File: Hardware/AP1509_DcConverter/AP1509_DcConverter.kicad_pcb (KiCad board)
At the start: 4 copper layers, 34 x 34 mm, 17 parts, among them J2 01x02, J3 01x03, U1 AP1509

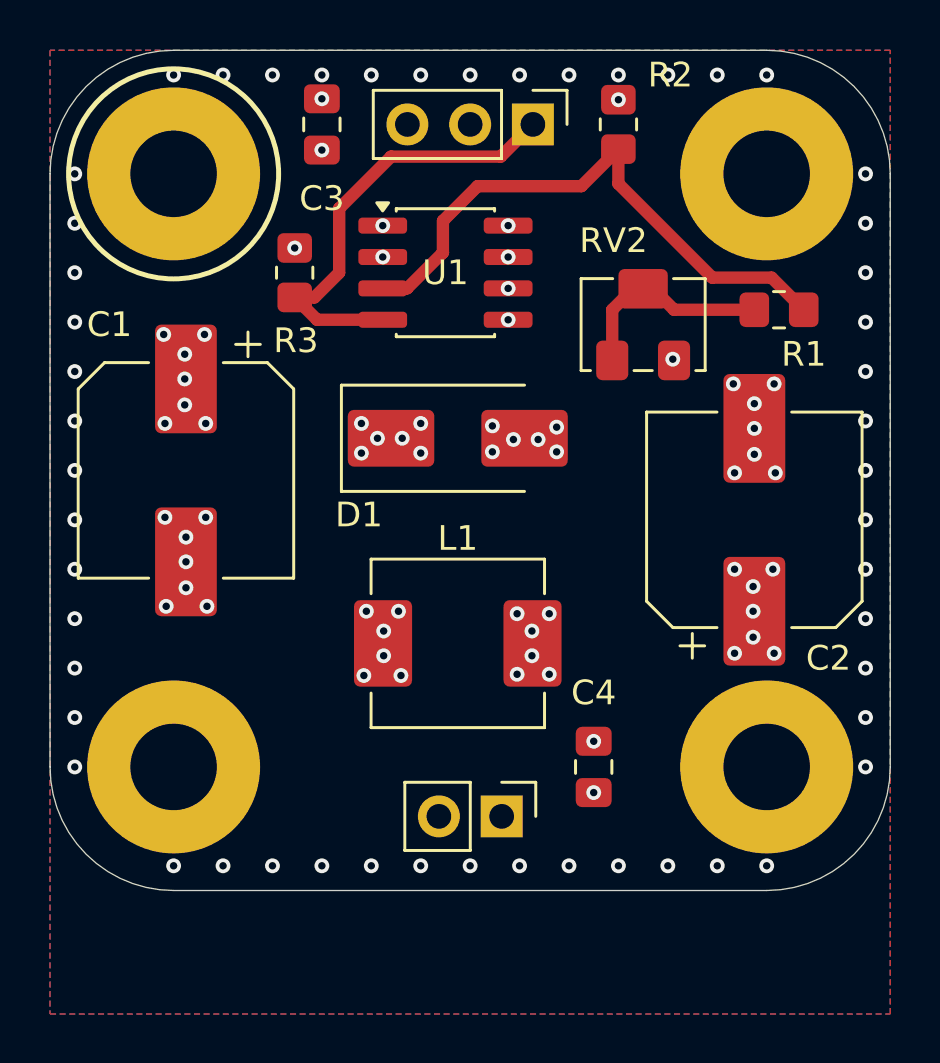
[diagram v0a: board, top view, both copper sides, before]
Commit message: Hardware updates. Add Lr04 lora module datasheets
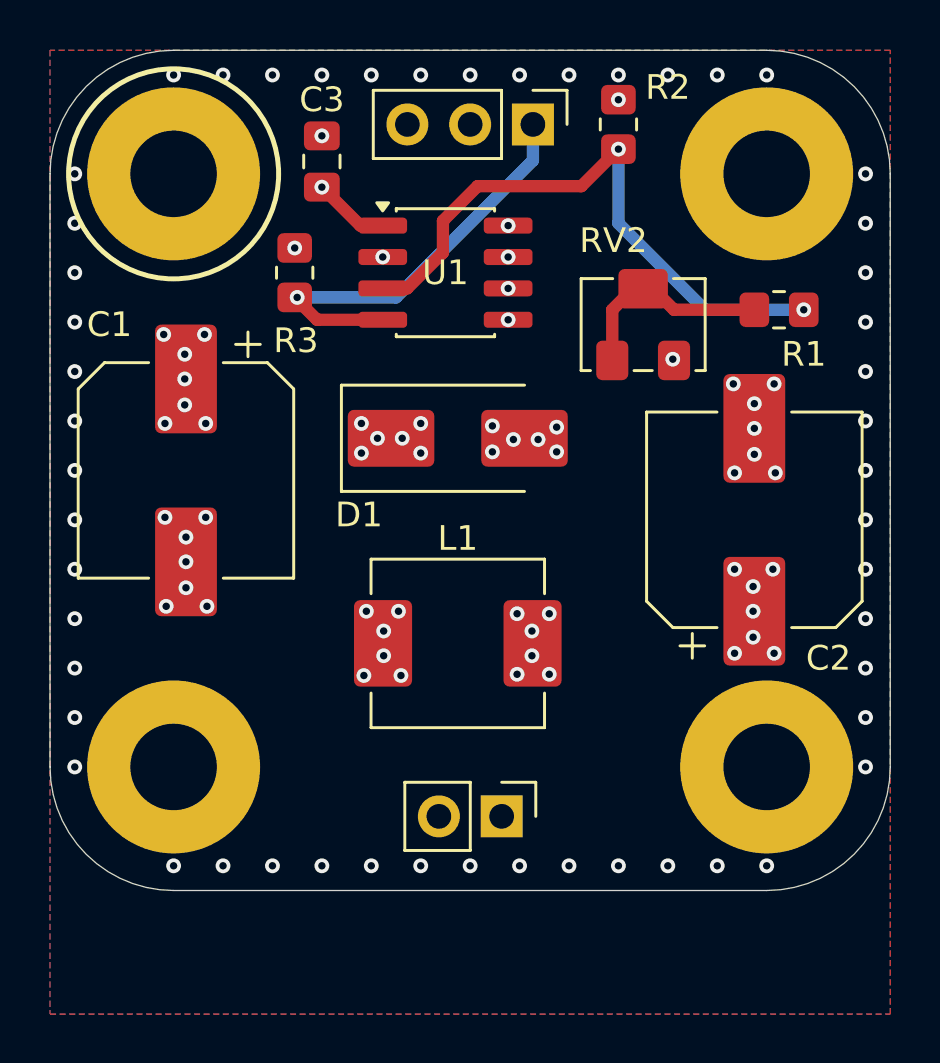
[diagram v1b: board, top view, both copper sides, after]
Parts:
- removed C4: 0.1uF, Capacitor_SMD:C_0805_2012Metric_Pad1.18x1.45mm_HandSolder
- moved C3 1.50 mm to (134.0, 63.5)
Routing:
- net Net-(J3-Pin_3): track 0.00 -> 3.11 mm, vias 9 -> 8
- net Net-(U1-FB): track 23.6 -> 24.6 mm, vias 0 -> 2
- net Net-(J3-Pin_1): track 18.0 -> 17.3 mm, vias 0 -> 1
- net Net-(J2-Pin_1): vias 15 -> 14
- net GND: vias 80 -> 79
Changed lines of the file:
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@@
 	(paper "A4")
 	(layers
-		(0 "F.Cu" signal "Traces")
+		(0 "F.Cu" signal "F.Signal-Ground")
 		(4 "In1.Cu" power "Ground")
 		(6 "In2.Cu" mixed "Power")
-		(2 "B.Cu" power "Ground2")
+		(2 "B.Cu" power "B.Signal-Ground")
 		(5 "F.SilkS" user "F.Silkscreen")
 		(7 "B.SilkS" user "B.Silkscreen")
@@
 				(type "Top Silk Screen")
 			)
-			(layer "F.Paste"
-				(type "Top Solder Paste")
-			)
 			(layer "F.Mask"
 				(type "Top Solder Mask")
@@
 				(thickness 0.01)
 			)
-			(layer "B.Paste"
-				(type "Bottom Solder Paste")
-			)
 			(layer "B.SilkS"
 				(type "Bottom Silk Screen")
@@
 	(footprint "Capacitor_SMD:C_0805_2012Metric_Pad1.18x1.45mm_HandSolder"
 		(layer "F.Cu")
-		(at 134 62 90)
+		(at 134 63.5 90)
 		(descr "Capacitor SMD 0805 (2012 Metric), square (rectangular) end terminal, IPC-7351 nominal with elongated pad for handsoldering. (Body size source: IPC-SM-782 page 76, https://www.pcb-3d.com/wordpress/wp-content/uploads/ipc-sm-782a_amendment_1_and_2.pdf, https://docs.google.com/spreadsheets/d/1BsfQQcO9C6DZCsRaXUlFlo91Tg2WpOkGARC1WS5S8t0/edit?usp=sharing), generated with kicad-footprint-generator")
 		(tags "capacitor handsolder")
 		(property "Reference" "C3"
-			(at -3 0 180)
+			(at 2.5 0 180)
 			(layer "F.SilkS")
 			(effects
@@
 		(embedded_fonts no)
 	)
-	(footprint "Capacitor_SMD:C_0805_2012Metric_Pad1.18x1.45mm_HandSolder"
-		(layer "F.Cu")
-		(at 145 88 90)
-		(descr "Capacitor SMD 0805 (2012 Metric), square (rectangular) end terminal, IPC-7351 nominal with elongated pad for handsoldering. (Body size source: IPC-SM-782 page 76, https://www.pcb-3d.com/wordpress/wp-content/uploads/ipc-sm-782a_amendment_1_and_2.pdf, https://docs.google.com/spreadsheets/d/1BsfQQcO9C6DZCsRaXUlFlo91Tg2WpOkGARC1WS5S8t0/edit?usp=sharing), generated with kicad-footprint-generator")
-		(tags "capacitor handsolder")
-		(property "Reference" "C4"
-			(at 3 0 0)
-			(layer "F.SilkS")
-			(effects
-				(font
-					(size 1 1)
-					(thickness 0.15)
-				)
-			)
-		)
-		(property "Value" "0.1uF"
-			(at 0 1.68 90)
-			(layer "F.Fab")
-			(effects
-				(font
-					(size 1 1)
-					(thickness 0.15)
-				)
-			)
-		)
-		(property "Datasheet" "~"
-			(at 0 0 90)
-			(layer "F.Fab")
-			(hide yes)
-			(effects
-				(font
-					(size 1.27 1.27)
-					(thickness 0.15)
-				)
-			)
-		)
-		(property "Description" "Unpolarized capacitor"
-			(at 0 0 90)
-			(layer "F.Fab")
-			(hide yes)
-			(effects
-				(font
-					(size 1.27 1.27)
-					(thickness 0.15)
-				)
-			)
-		)
-		(property ki_fp_filters "C_*")
-		(sheetname "/")
-		(sheetfile "AP1509_DcConverter.kicad_sch")
-		(attr smd)
-		(fp_line
-			(start -0.261252 -0.735)
-			(end 0.261252 -0.735)
-			(stroke
-				(width 0.12)
-				(type solid)
-			)
-			(layer "F.SilkS")
-		)
-		(fp_line
-			(start -0.261252 0.735)
-			(end 0.261252 0.735)
-			(stroke
-				(width 0.12)
-				(type solid)
-			)
-			(layer "F.SilkS")
-		)
-		(fp_rect
-			(start -1.88 -0.98)
-			(end 1.88 0.98)
-			(stroke
-				(width 0.05)
-				(type solid)
-			)
-			(fill no)
-			(layer "F.CrtYd")
-		)
-		(fp_rect
-			(start -1 -0.625)
-			(end 1 0.625)
-			(stroke
-				(width 0.1)
-				(type solid)
-			)
-			(fill no)
-			(layer "F.Fab")
-		)
-		(fp_text user "${REFERENCE}"
-			(at 0 0 90)
-			(layer "F.Fab")
-			(effects
-				(font
-					(size 0.5 0.5)
-					(thickness 0.08)
-				)
-			)
-		)
-		(pad "1" smd roundrect
-			(at -1.0375 0 90)
-			(size 1.175 1.45)
-			(layers "F.Cu" "F.Mask" "F.Paste")
-			(roundrect_rratio 0.212766)
-			(net 2 "Net-(J2-Pin_1)")
-			(pintype "passive")
-		)
-		(pad "2" smd roundrect
-			(at 1.0375 0 90)
-			(size 1.175 1.45)
-			(layers "F.Cu" "F.Mask" "F.Paste")
-			(roundrect_rratio 0.212766)
-			(net 1 "GND")
-			(pintype "passive")
-		)
-		(embedded_fonts no)
-		(model "${KICAD9_3DMODEL_DIR}/Capacitor_SMD.3dshapes/C_0805_2012Metric.step"
-			(offset
-				(xyz 0 0 0)
-			)
-			(scale
-				(xyz 1 1 1)
-			)
-			(rotate
-				(xyz 0 0 0)
-			)
-		)
-	)
 	(footprint "MountingHole:MountingHole_3.5mm_Pad"
 		(layer "F.Cu")
@@
 		(tags "resistor handsolder")
 		(property "Reference" "R2"
-			(at -2 -2.1 0)
+			(at -1.5 -2 0)
 			(layer "F.SilkS")
 			(effects
@@
 		)
 	)
-	(gr_text "AP1509 DC Converter\nrev. B"
+	(gr_text "AP1509\nDC Converter\nrev. B"
 		(at 140 75.825 0)
 		(layer "B.SilkS")
@@
 	)
 	(via
-		(at 134 60.9625)
-		(size 0.6)
-		(drill 0.3)
-		(layers "F.Cu" "B.Cu")
-		(net 1)
-	)
-	(via
 		(at 134 60)
 		(size 0.6)
@@
 	)
 	(via
-		(at 145 86.9625)
-		(size 0.6)
-		(drill 0.3)
-		(layers "F.Cu" "B.Cu")
-		(net 1)
-	)
-	(via
 		(at 146 92)
 		(size 0.6)
@@
 	)
 	(via
+		(at 134 62.4625)
+		(size 0.6)
+		(drill 0.3)
+		(layers "F.Cu" "B.Cu")
+		(net 1)
+	)
+	(via
 		(at 143.5 75.25)
 		(size 0.6)
@@
 	)
 	(via
-		(at 145 89.0375)
-		(size 0.6)
-		(drill 0.3)
-		(layers "F.Cu" "B.Cu")
-		(net 2)
-	)
-	(via
 		(at 151.45 80.7)
 		(size 0.6)
@@
 		(net 3)
 	)
+	(segment
+		(start 135.5575 66.095)
+		(end 134 64.5375)
+		(width 0.5)
+		(layer "F.Cu")
+		(net 4)
+	)
+	(segment
+		(start 136.4625 66.095)
+		(end 135.5575 66.095)
+		(width 0.5)
+		(layer "F.Cu")
+		(net 4)
+	)
 	(via
-		(at 127.6 70.5)
+		(at 134 64.5375)
 		(size 0.6)
 		(drill 0.3)
@@
 	)
 	(via
-		(at 136.4625 66.095)
+		(at 127.6 70.5)
 		(size 0.6)
 		(drill 0.3)
@@
 	)
 	(via
-		(at 134 63.0375)
-		(size 0.6)
-		(drill 0.3)
-		(layers "F.Cu" "B.Cu")
-		(net 4)
-	)
-	(via
 		(at 129.25 70.5)
 		(size 0.6)
@@
 	)
 	(segment
-		(start 146 64.4)
-		(end 146 63)
-		(width 0.5)
-		(layer "F.Cu")
-		(net 5)
-	)
-	(segment
 		(start 138.9 65.9)
 		(end 140.3 64.5)
@@
 	)
 	(segment
-		(start 153.5 69.5)
-		(end 152.2 68.2)
-		(width 0.5)
-		(layer "F.Cu")
-		(net 5)
-	)
-	(segment
 		(start 136.4625 68.635)
 		(end 137.449999 68.635)
@@
 	)
 	(segment
-		(start 149.8 68.2)
-		(end 146 64.4)
+		(start 137.449999 68.635)
+		(end 138.9 67.184999)
 		(width 0.5)
 		(layer "F.Cu")
 		(net 5)
 	)
+	(via
+		(at 153.5 69.5)
+		(size 0.6)
+		(drill 0.3)
+		(layers "F.Cu" "B.Cu")
+		(net 5)
+	)
+	(via
+		(at 146 63)
+		(size 0.6)
+		(drill 0.3)
+		(layers "F.Cu" "B.Cu")
+		(net 5)
+	)
 	(segment
-		(start 152.2 68.2)
-		(end 149.8 68.2)
+		(start 149.5 69.5)
+		(end 146 66)
 		(width 0.5)
-		(layer "F.Cu")
+		(layer "B.Cu")
 		(net 5)
 	)
 	(segment
-		(start 137.449999 68.635)
-		(end 138.9 67.184999)
+		(start 153.5 69.5)
+		(end 149.5 69.5)
 		(width 0.5)
-		(layer "F.Cu")
+		(layer "B.Cu")
 		(net 5)
 	)
 	(segment
-		(start 133.7 69)
-		(end 134.7 68)
+		(start 146 66)
+		(end 146 63)
 		(width 0.5)
-		(layer "F.Cu")
-		(net 6)
+		(layer "B.Cu")
+		(net 5)
 	)
 	(segment
-		(start 136.799 63.301)
-		(end 141.239 63.301)
+		(start 136.4625 69.905)
+		(end 133.805 69.905)
 		(width 0.5)
 		(layer "F.Cu")
@@
 	)
 	(segment
-		(start 132.9 69)
-		(end 133.7 69)
+		(start 133.805 69.905)
+		(end 132.9 69)
 		(width 0.5)
 		(layer "F.Cu")
 		(net 6)
 	)
-	(segment
-		(start 134.7 65.4)
-		(end 136.799 63.301)
-		(width 0.5)
-		(layer "F.Cu")
+	(via
+		(at 133 69)
+		(size 0.6)
+		(drill 0.3)
+		(layers "F.Cu" "B.Cu")
 		(net 6)
 	)
 	(segment
-		(start 141.239 63.301)
-		(end 142.54 62)
+		(start 132.9 69)
+		(end 133 69)
 		(width 0.5)
-		(layer "F.Cu")
+		(layer "B.Cu")
 		(net 6)
 	)
 	(segment
-		(start 136.4625 69.905)
-		(end 133.805 69.905)
+		(start 142.54 63.46)
+		(end 142.54 62)
 		(width 0.5)
-		(layer "F.Cu")
+		(layer "B.Cu")
 		(net 6)
 	)
 	(segment
-		(start 133.805 69.905)
-		(end 132.9 69)
+		(start 133 69)
+		(end 137 69)
 		(width 0.5)
-		(layer "F.Cu")
+		(layer "B.Cu")
 		(net 6)
 	)
 	(segment
-		(start 134.7 68)
-		(end 134.7 65.4)
+		(start 137 69)
+		(end 142.54 63.46)
 		(width 0.5)
-		(layer "F.Cu")
+		(layer "B.Cu")
 		(net 6)
 	)
